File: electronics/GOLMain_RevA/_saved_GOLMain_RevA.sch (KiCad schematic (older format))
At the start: 31 parts, among them P1 CONN_LEDS, P2 CONN_SERIAL, P3 CONN_READERS, P4 CONN_POWER, Q1 BSS138, Q2 BSS138, SW1 SW_PUSH, SW2 SW_PUSH, U1 LM1117-3.3, U2 ESP8266-12E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

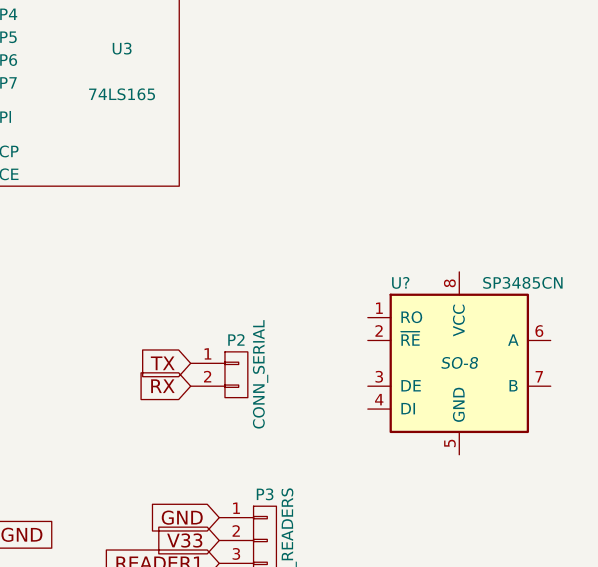
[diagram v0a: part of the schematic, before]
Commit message: added initial bill of materials mostly consisting of the electronics and power systems with estimated parts list
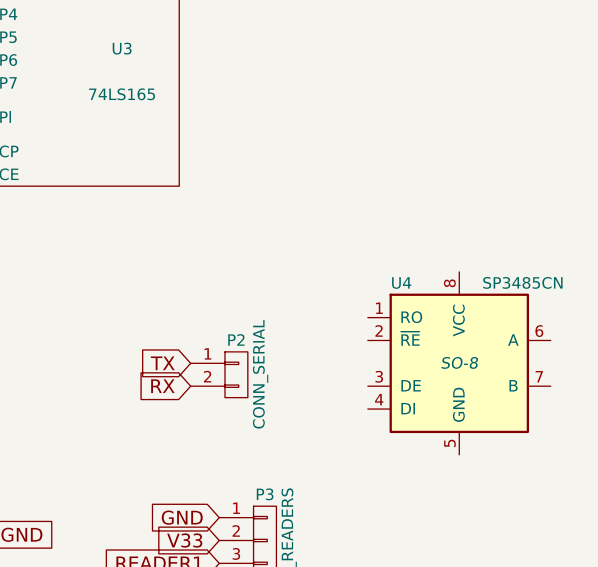
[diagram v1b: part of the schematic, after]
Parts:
- gave numbers to parts that had none: 1
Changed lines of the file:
@@
 V33
 $Comp
-L +3.3V #PWR01
+L +3.3V #PWR3
 U 1 1 58B19A2F
 P 3550 1750
-F 0 "#PWR01" H 3550 1600 50  0001 C CNN
+F 0 "#PWR3" H 3550 1600 50  0001 C CNN
 F 1 "+3.3V" H 3550 1890 50  0000 C CNN
 F 2 "" H 3550 1750 50  0000 C CNN
@@
 $EndComp
 $Comp
-L GND #PWR02
+L GND #PWR2
 U 1 1 58B19D95
 P 3000 2475
-F 0 "#PWR02" H 3000 2225 50  0001 C CNN
+F 0 "#PWR2" H 3000 2225 50  0001 C CNN
 F 1 "GND" H 3000 2325 50  0000 C CNN
 F 2 "" H 3000 2475 50  0000 C CNN
@@
 $EndComp
 $Comp
-L +12V #PWR03
+L +12V #PWR1
 U 1 1 58B19DE8
 P 2775 1825
-F 0 "#PWR03" H 2775 1675 50  0001 C CNN
+F 0 "#PWR1" H 2775 1675 50  0001 C CNN
 F 1 "+12V" H 2775 1965 50  0000 C CNN
 F 2 "" H 2775 1825 50  0000 C CNN
@@
 Connection ~ 3000 2350
 $Comp
-L VCC #PWR04
+L VCC #PWR4
 U 1 1 58B1A133
 P 3750 1750
-F 0 "#PWR04" H 3750 1600 50  0001 C CNN
+F 0 "#PWR4" H 3750 1600 50  0001 C CNN
 F 1 "VCC" H 3750 1900 50  0000 C CNN
 F 2 "" H 3750 1750 50  0000 C CNN
@@
 Connection ~ 2775 2350
 $Comp
-L SP3485CN U?
+L SP3485CN U4
 U 1 1 58B21144
 P 7575 3250
-F 0 "U?" H 7275 3600 50  0000 L CNN
+F 0 "U4" H 7275 3600 50  0000 L CNN
 F 1 "SP3485CN" H 7675 3600 50  0000 L CNN
 F 2 "SO-8" H 7575 3250 50  0000 C CIN
